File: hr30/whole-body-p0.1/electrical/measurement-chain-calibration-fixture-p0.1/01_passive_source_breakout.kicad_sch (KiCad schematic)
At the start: 3 parts

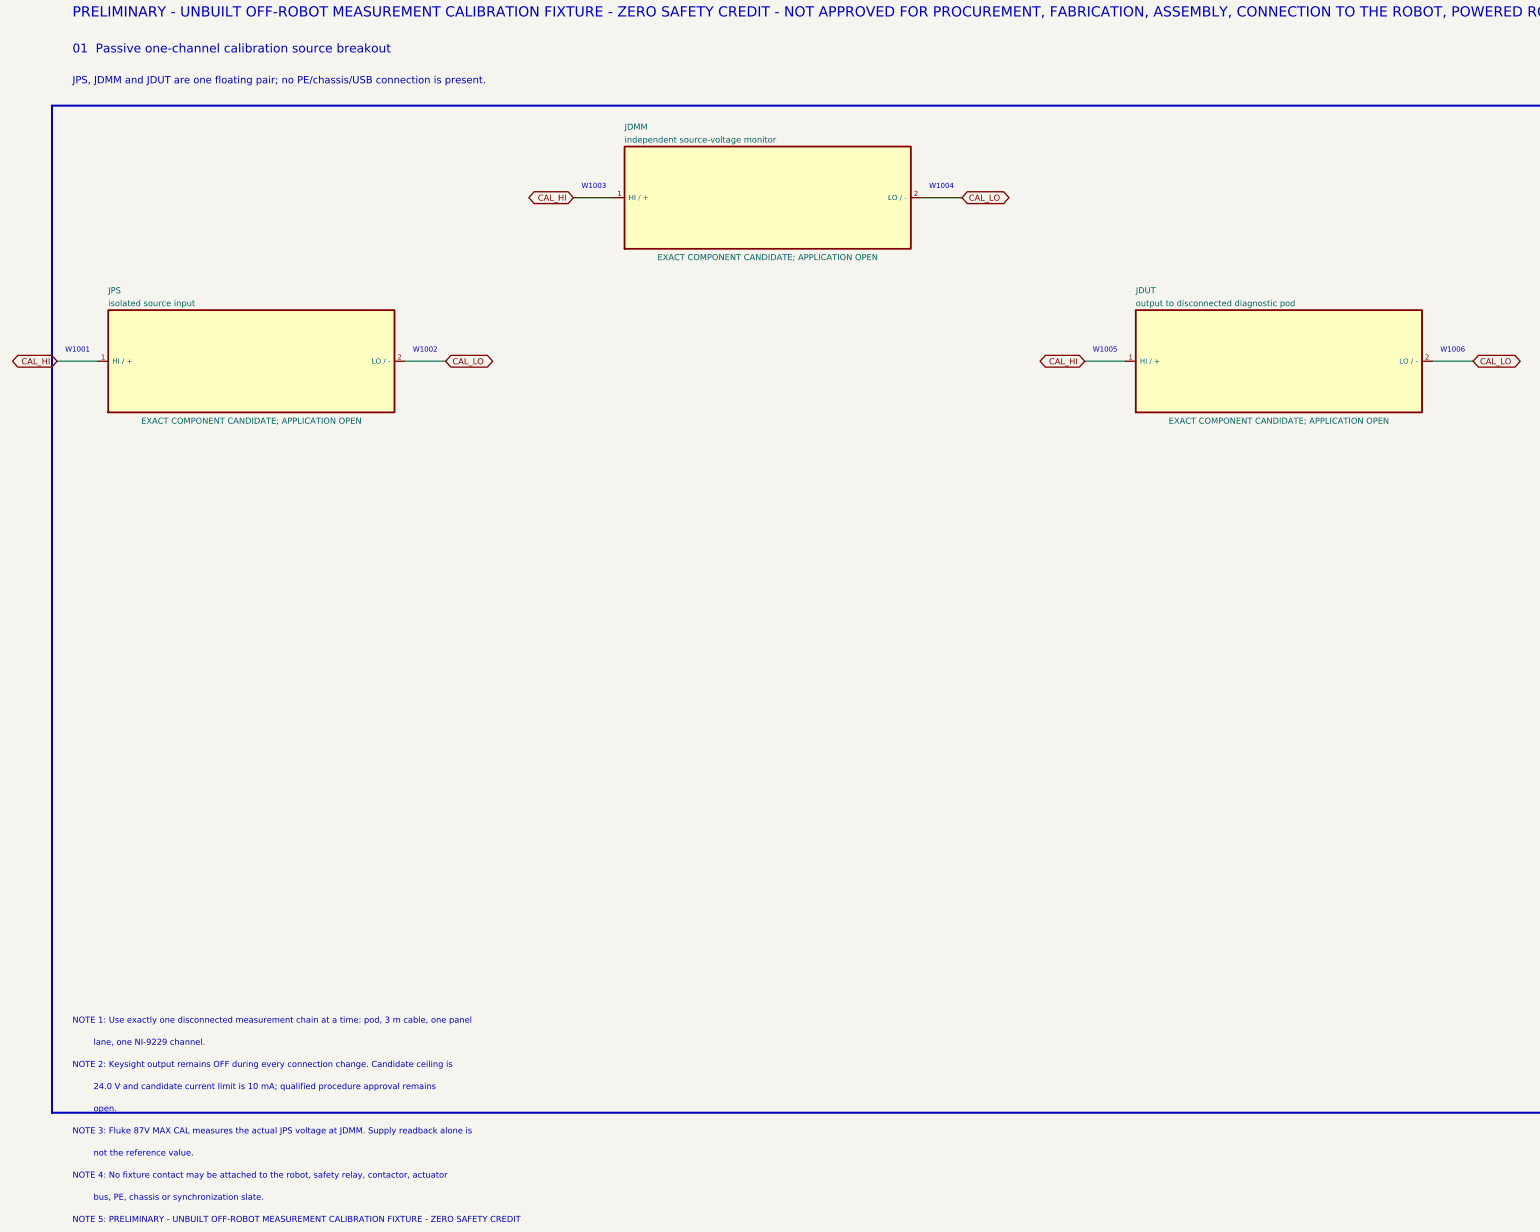
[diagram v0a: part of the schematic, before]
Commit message: Add HR-30 calibration cable and fault-adapter kit
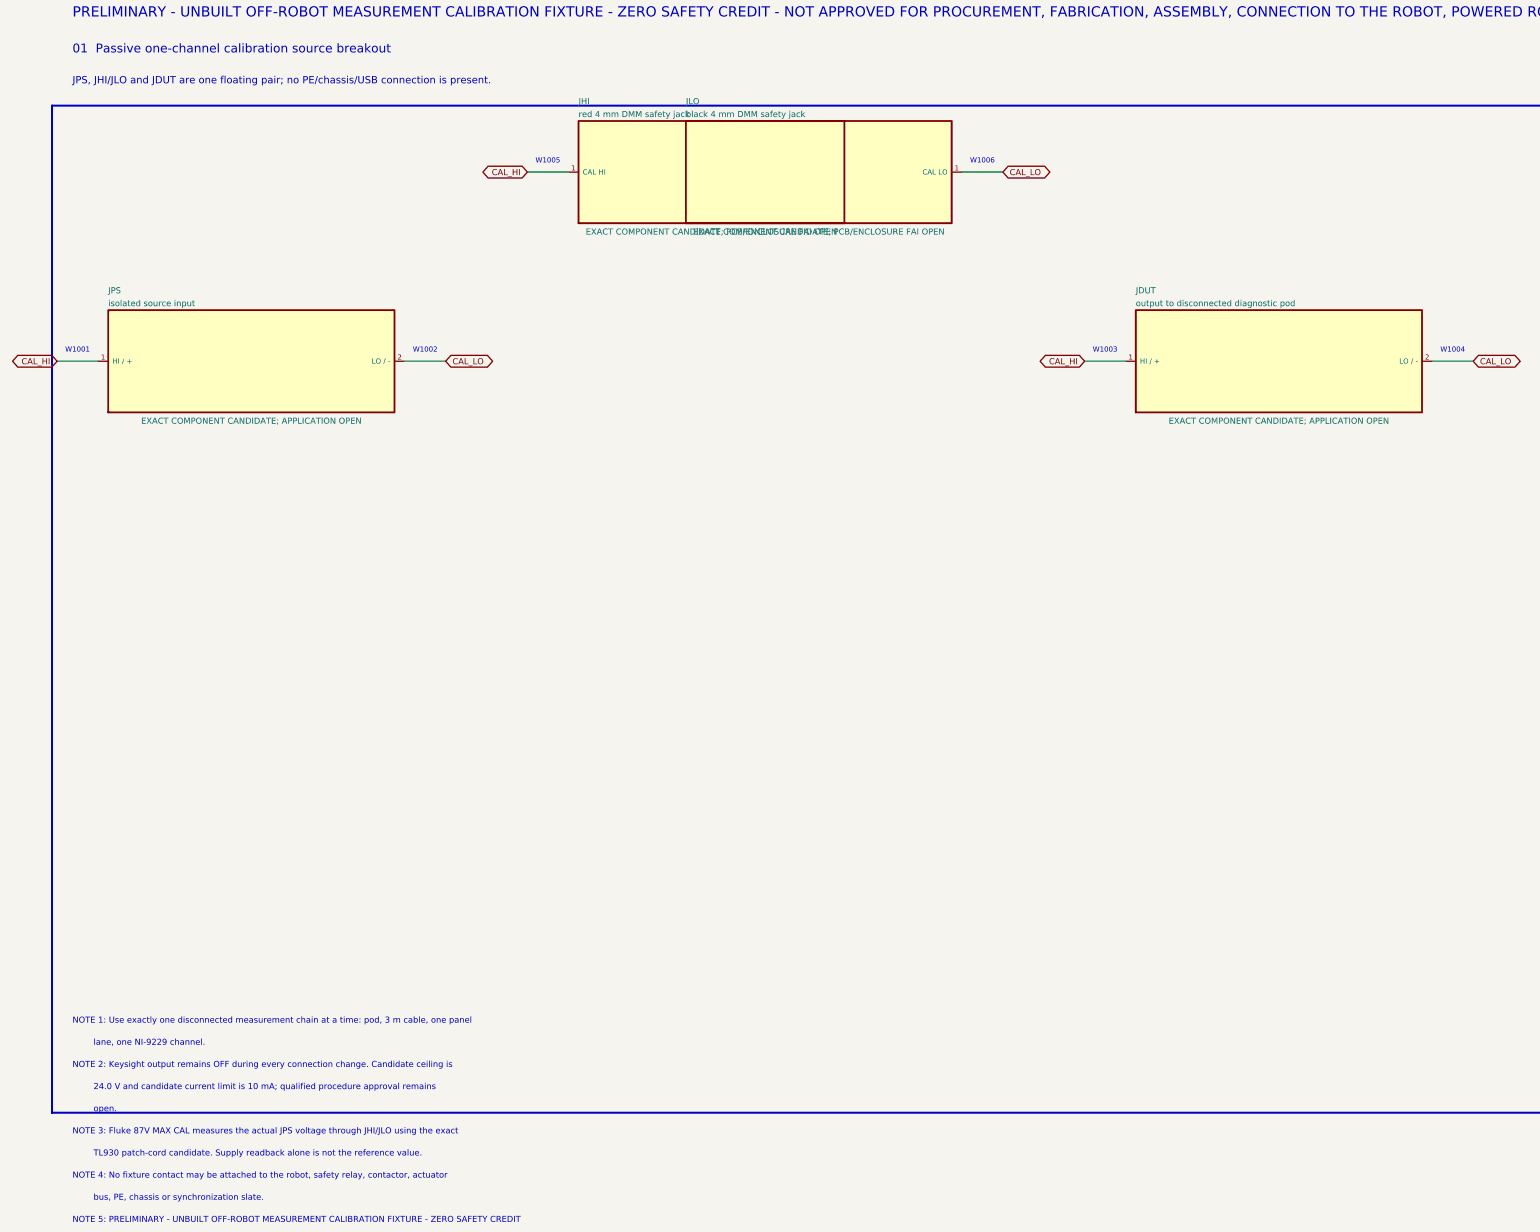
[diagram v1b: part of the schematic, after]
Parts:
- removed JDMM: independent source-voltage monitor, Connector_Phoenix_MSTB:PhoenixContact_MSTBA_2,5_2-G-5,08_1x02_P5.08mm_Horizontal, symbol PBV3:JDMM
- added JHI: red 4 mm DMM safety jack, HR30_CAL:POMONA_73099, symbol PBV3:JHI
- added JLO: black 4 mm DMM safety jack, HR30_CAL:POMONA_73099, symbol PBV3:JLO
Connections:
- net CAL_HI: now also JHI.1 (CAL HI)
- net CAL_LO: now also JLO.1 (CAL LO)
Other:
- note added: "JPS, JHI/JLO and JDUT are one floating pair; no PE/chassis/USB connection is present."
- note added: "NOTE 3: Fluke 87V MAX CAL measures the actual JPS voltage through JHI/JLO using the exact"
- note added: "TL930 patch-cord candidate. Supply readback alone is not the reference value."
- note removed: "JPS, JDMM and JDUT are one floating pair; no PE/chassis/USB connection is present."
- note removed: "NOTE 3: Fluke 87V MAX CAL measures the actual JPS voltage at JDMM. Supply readback alone is"
- note removed: "not the reference value."
